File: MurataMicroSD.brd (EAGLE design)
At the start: 60 x 68 mm, 15 parts, among them U1 IC_BLE_LBCA2HNZYZ-711

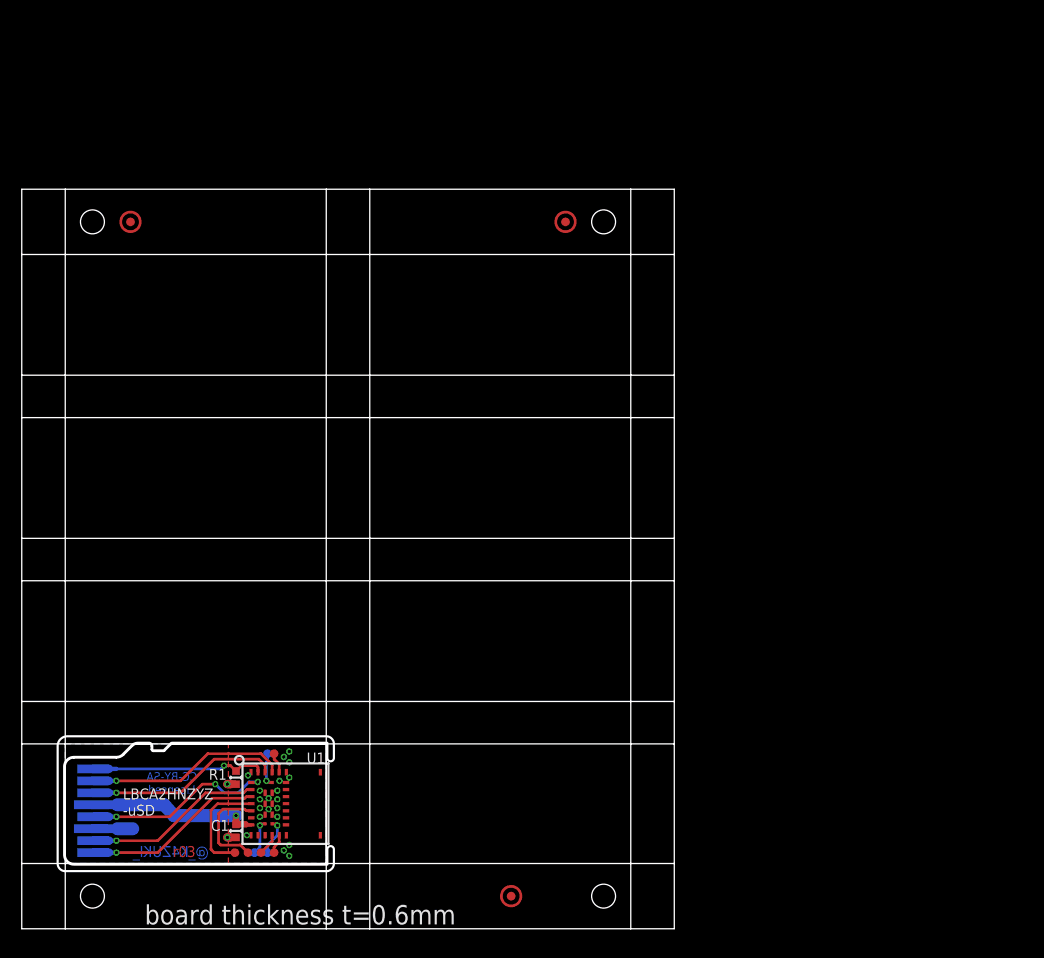
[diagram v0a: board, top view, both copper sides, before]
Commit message: [ FIX ] library update; add debug connector
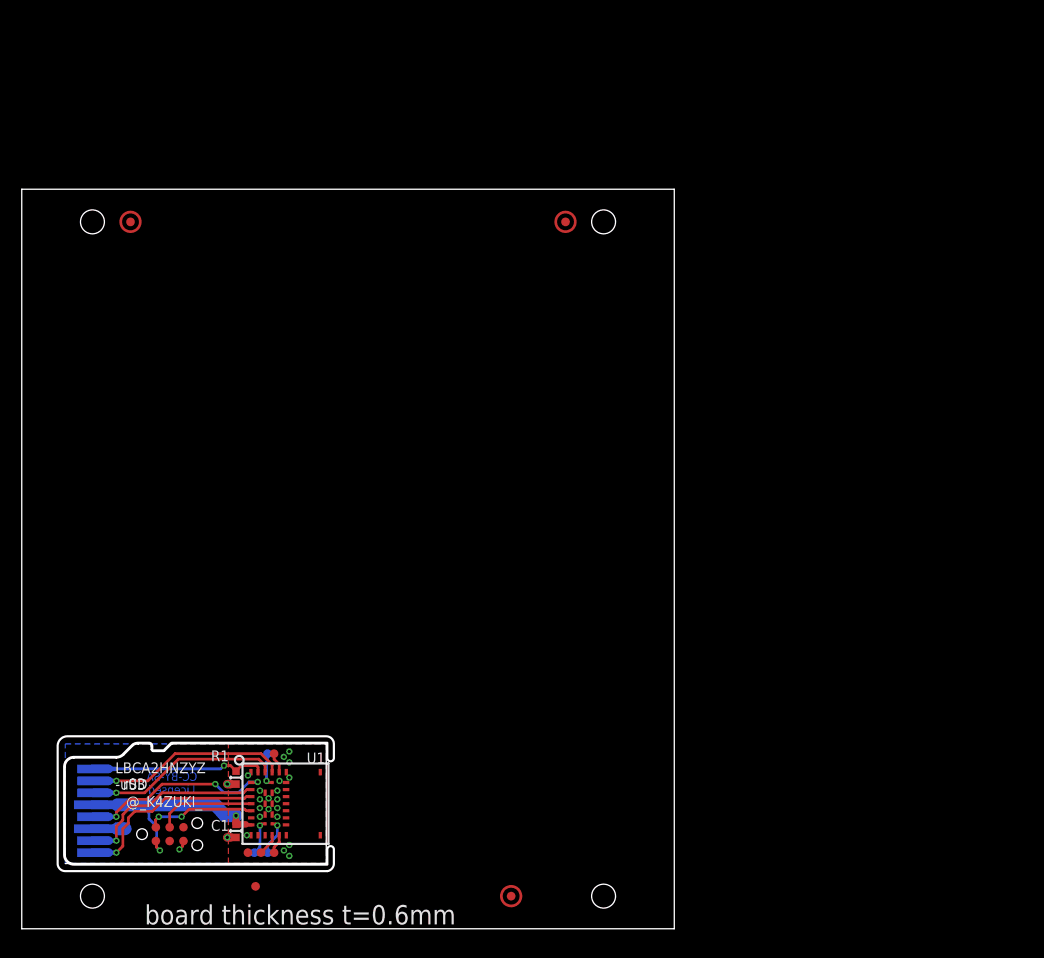
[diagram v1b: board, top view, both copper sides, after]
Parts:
- added CON1: CON_TC2030-CTL-NL, mylib:CON_TC2030-IDC-NL
- moved TP1 3.64 mm to (21.5, 3.90)
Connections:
- net 3.3V: now also CON1.1
- net GND: now also CON1.5
- net SWCLK: now also CON1.4
- net SWDIO: now also CON1.2
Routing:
- net 3.3V: track 16.0 -> 22.6 mm, vias 1 -> 2
- net DAT1: track 16.7 -> 17.9 mm
- net MISO: track 16.5 -> 17.6 mm
- net SWDIO: track 9.00 -> 10.0 mm, vias 0 -> 2
- net SWCLK: track 9.87 -> 9.24 mm
- net GND: track 5.40 -> 5.62 mm, vias 22 -> 23
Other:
- outline, holes or cut-outs redrawn

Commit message: [ uSD ] add 'Open Source Hardware' silk
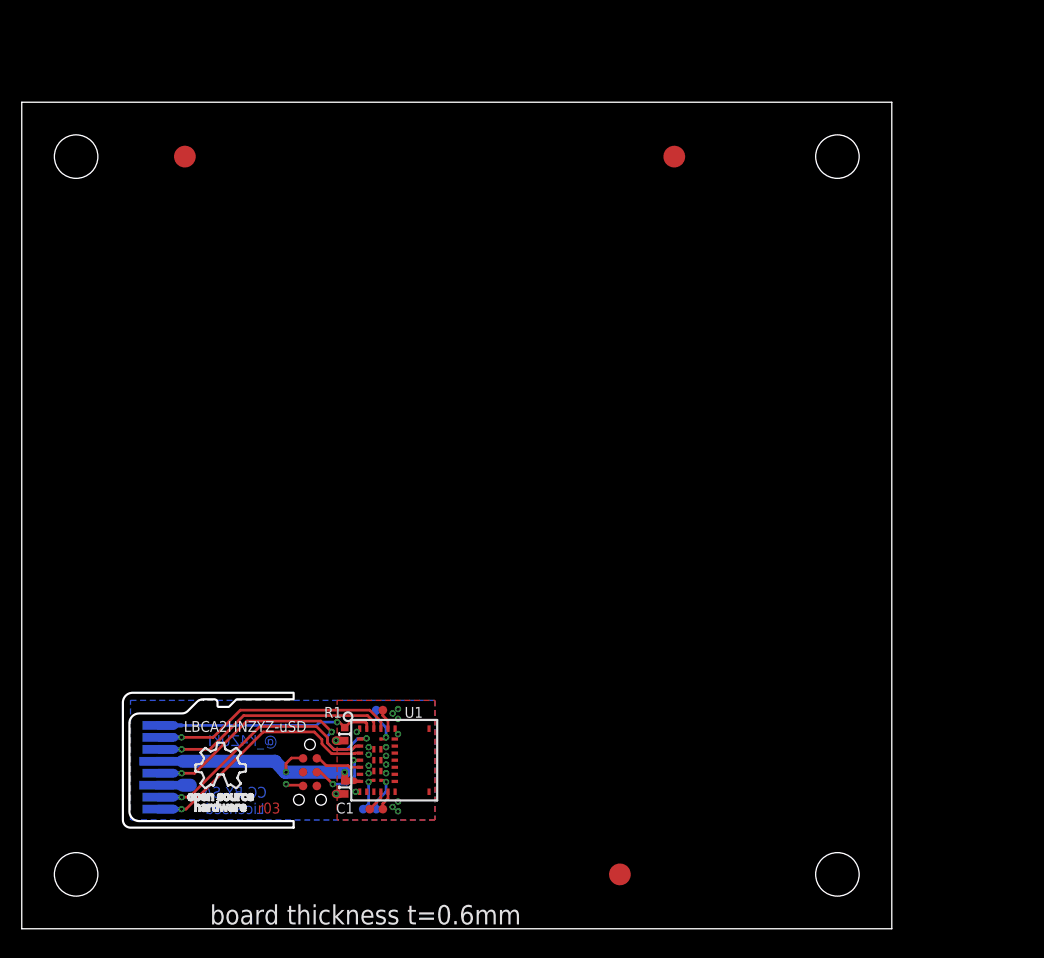
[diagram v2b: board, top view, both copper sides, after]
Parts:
- removed TP1, TP2: TPTP08R, testpad_local:TP08R
- TP3, TP4, TP5: value TPTP08R -> TPTP20R; device testpad_local:TP08R -> testpad_local:TP20R
- moved CON1 14.1 mm to (26.5, 14.4), turned to 270 degrees
- moved TP5 11.7 mm to (60.0, 71.0)
- moved TP8 10.8 mm to (33.2, 11.0)
- moved TP9 10.8 mm to (33.2, 20.1)
- moved C1 10.8 mm to (29.7, 13.0)
- moved TP10 10.8 mm to (32.6, 20.1)
- moved TP11 10.8 mm to (31.4, 11.0)
- moved TP6 10.8 mm to (32.6, 11.0)
- moved TP7 10.8 mm to (32.0, 11.0)
- moved U1 10.8 mm to (30.5, 19.0)
- moved R1 10.8 mm to (29.7, 17.9)
- moved TP4 10.2 mm to (55.0, 5.00)
- moved TP3 7.81 mm to (15.0, 71.0)
- moved C100 7.21 mm to (10.0, 21.0)
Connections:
- net SWCLK: no longer TP1.TP
- net SWDIO: no longer TP2.TP
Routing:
- net SCK: track 18.0 -> 24.4 mm
- net SWDIO: track 10.0 -> 4.33 mm, vias 2 -> 0
- net MISO: track 17.6 -> 22.5 mm
- net DAT1: track 17.9 -> 22.6 mm
- net RXD_MOSI: track 18.0 -> 22.0 mm
- net !CS!: track 18.6 -> 22.6 mm
- net N$1: track 16.2 -> 20.2 mm
- net SWCLK: track 9.24 -> 6.46 mm, vias 0 -> 2
- net GND: track 5.62 -> 6.43 mm, vias 23 -> 20
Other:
- board size 60 x 68 mm -> 80 x 76 mm
- board text added: "LBCA2HNZYZ-uSD"
- board text removed: "LBCA2HNZYZ -uSD"

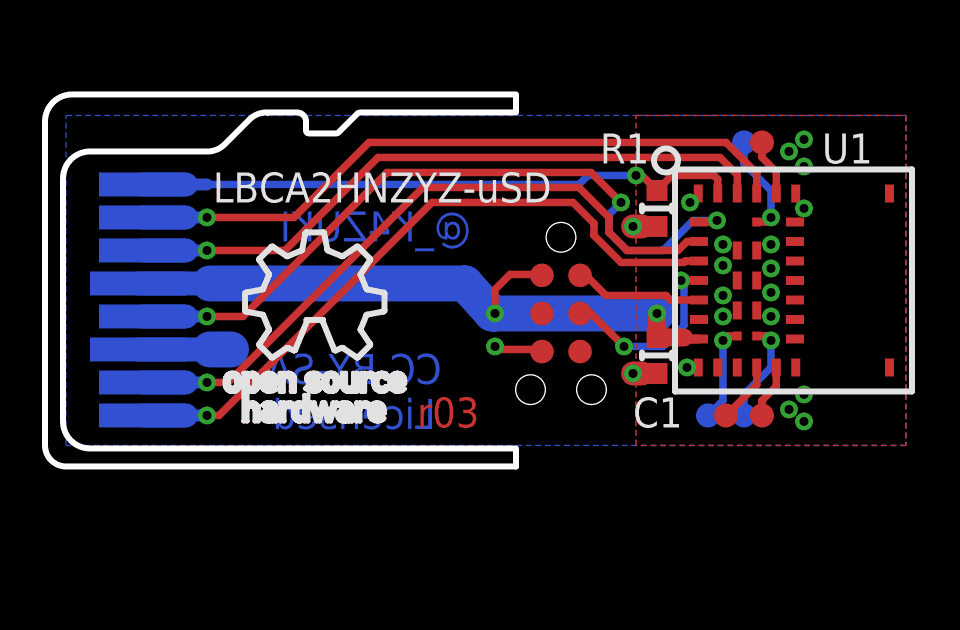
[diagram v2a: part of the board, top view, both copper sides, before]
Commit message: [ uSD ] uSD pin 8 is replaced to Vpp
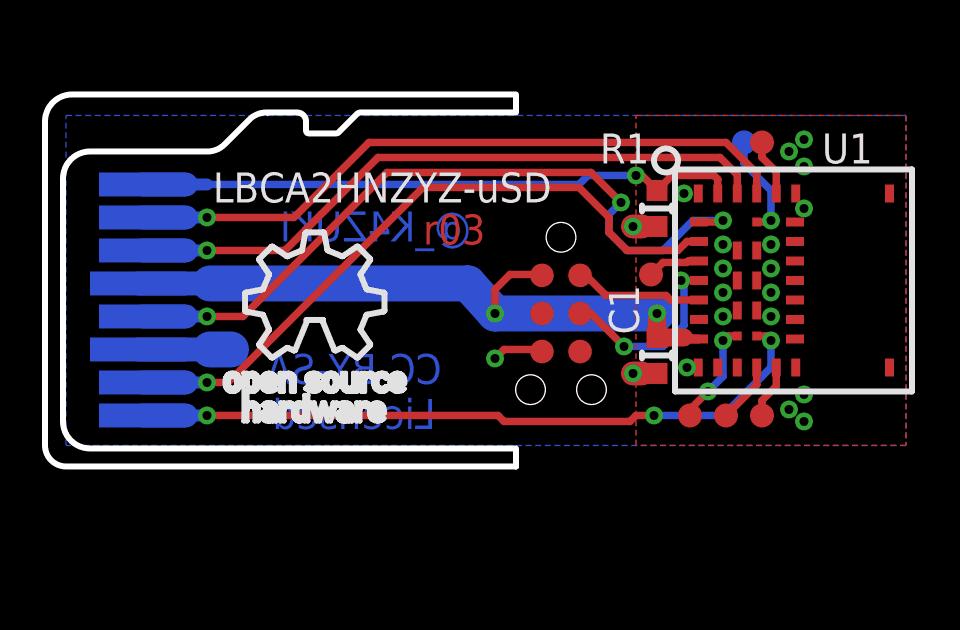
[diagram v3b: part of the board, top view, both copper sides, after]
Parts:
- removed TP6: TPTP08R, testpad_local:TP08R
- added TP1: TPTP08R, testpad_local:TP08R
- moved TP11 0.60 mm to (30.8, 11.0), flipped to the top
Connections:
- net DAT1: now also TP1.TP; no longer C100.8_DAT1
- net N$2: now also C100.8_DAT1; no longer TP6.TP
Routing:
- net DAT1: track 22.6 -> 1.79 mm, vias 1 -> 0
- net N$2: track 3.41 -> 23.2 mm, vias 1 -> 3
- net P1_1: track 3.24 -> 3.49 mm, vias 1 -> 2

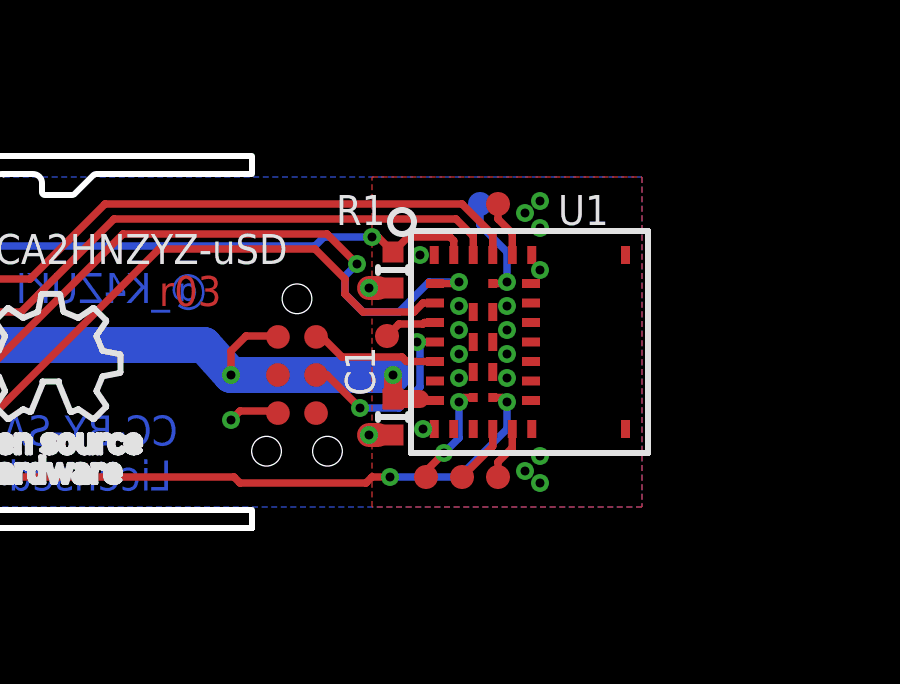
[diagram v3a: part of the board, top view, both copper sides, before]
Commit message: [ uSD ][ USB ] library update
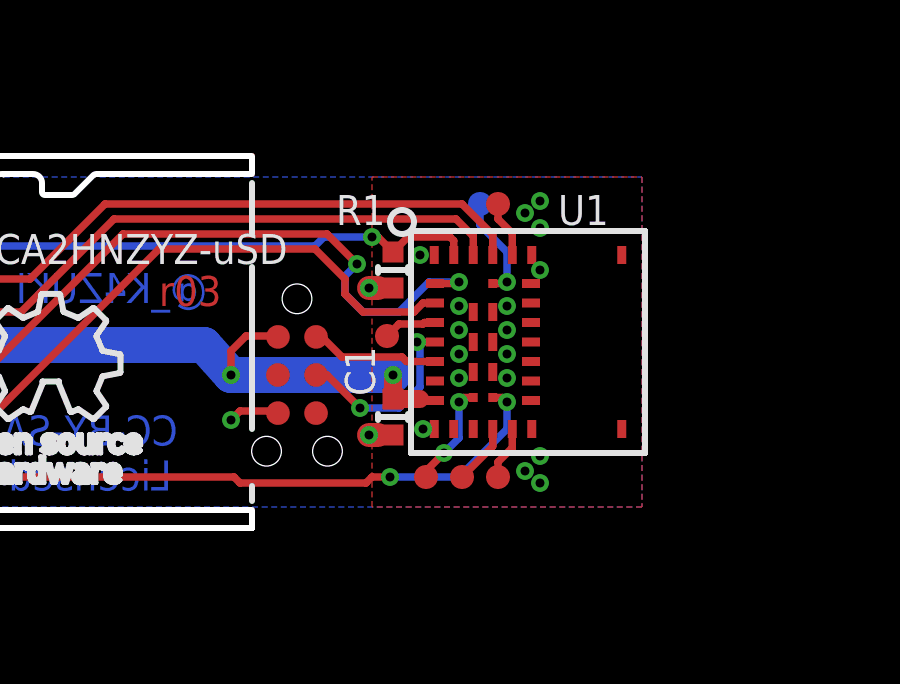
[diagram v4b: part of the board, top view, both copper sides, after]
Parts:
- renumbered TP3 to TP100, TP4 to TP101, TP5 to TP102
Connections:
- net DAT1 renamed P0_6
- net N$2 renamed VPP
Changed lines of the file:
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@@
 <layer number="45" name="Holes" color="7" fill="1" visible="yes" active="yes"/>
 <layer number="46" name="Milling" color="3" fill="0" visible="yes" active="yes"/>
-<layer number="47" name="Measures" color="7" fill="1" visible="yes" active="yes"/>
+<layer number="47" name="Measures" color="7" fill="1" visible="no" active="yes"/>
 <layer number="48" name="Document" color="7" fill="1" visible="no" active="yes"/>
 <layer number="49" name="Reference" color="7" fill="1" visible="no" active="yes"/>
@@
 <wire x1="38" y1="40" x2="38" y2="76" width="0.8" layer="102"/>
 <text x="17.3" y="0.4" size="1.778" layer="25">board thickness t=0.6mm</text>
-<circle x="4" y="30" radius="0.1" width="0.1" layer="51"/>
-<circle x="4" y="45" radius="0.1" width="0.1" layer="51"/>
-<circle x="4" y="60" radius="0.1" width="0.1" layer="51"/>
-<circle x="32" y="60" radius="0.1" width="0.1" layer="51"/>
-<circle x="32" y="45" radius="0.1" width="0.1" layer="51"/>
 <wire x1="10" y1="55" x2="0" y2="55" width="0.8" layer="102"/>
 <wire x1="10" y1="55" x2="70" y2="55" width="0.8" layer="102"/>
 <wire x1="70" y1="55" x2="80" y2="55" width="0.8" layer="102"/>
-<circle x="32" y="30" radius="0.1" width="0.1" layer="51"/>
-<circle x="32" y="15" radius="0.1" width="0.1" layer="51"/>
 <hole x="5" y="5" drill="4"/>
 <hole x="75" y="5" drill="4"/>
@@
 <wire x1="18.944959375" y1="13.181640625" x2="18.55138125" y2="14.14558125" width="0.2" layer="21"/>
 <wire x1="18.55138125" y1="14.14558125" x2="18.566609375" y2="14.18416875" width="0.2" layer="21"/>
+<wire x1="25" y1="20.8" x2="25" y2="19.1" width="0.2" layer="21"/>
+<wire x1="25" y1="18" x2="25" y2="12.6" width="0.2" layer="21"/>
+<wire x1="25" y1="10.7" x2="25" y2="10.2" width="0.2" layer="21"/>
+<dimension x1="38" y1="10" x2="34.9" y2="10" x3="36.45" y3="7.7" textsize="0.999996875" textratio="20" layer="47"/>
 </plain>
 <attributes>
@@
 <attribute name="VALUE" x="31.6" y="17.3" size="1" layer="27" font="vector" ratio="20" rot="R90"/>
 </element>
-<element name="TP3" library="testpad_local" package="TP20R" value="TPTP20R" x="15" y="71" smashed="yes">
+<element name="TP100" library="testpad_local" package="TP20R" value="TPTP20R" x="15" y="71" smashed="yes">
 <attribute name="TP_SIGNAL_NAME" value="" x="15" y="69.095" size="1" layer="37"/>
 <attribute name="VALUE" x="14.619" y="70.619" size="0.0254" layer="27"/>
 </element>
-<element name="TP4" library="testpad_local" package="TP20R" value="TPTP20R" x="55" y="5" smashed="yes">
+<element name="TP101" library="testpad_local" package="TP20R" value="TPTP20R" x="55" y="5" smashed="yes">
 <attribute name="TP_SIGNAL_NAME" value="" x="55" y="3.095" size="1" layer="37"/>
 <attribute name="VALUE" x="54.619" y="4.619" size="0.0254" layer="27"/>
 </element>
-<element name="TP5" library="testpad_local" package="TP20R" value="TPTP20R" x="60" y="71" smashed="yes">
+<element name="TP102" library="testpad_local" package="TP20R" value="TPTP20R" x="60" y="71" smashed="yes">
 <attribute name="TP_SIGNAL_NAME" value="" x="60" y="69.095" size="1" layer="37"/>
 <attribute name="VALUE" x="59.619" y="70.619" size="0.0254" layer="27"/>
@@
 <wire x1="14.7" y1="12.1" x2="14" y2="12.1" width="0.4" layer="16"/>
 </signal>
-<signal name="DAT1">
+<signal name="P0_6">
 <contactref element="U1" pad="3"/>
 <contactref element="TP1" pad="TP"/>
@@
 <wire x1="28" y1="15" x2="30" y2="15" width="0.25" layer="1"/>
 </signal>
-<signal name="N$2">
+<signal name="VPP">
 <contactref element="U1" pad="31"/>
 <wire x1="33.025" y1="13.65" x2="33.35" y2="13.65" width="0.25" layer="1"/>

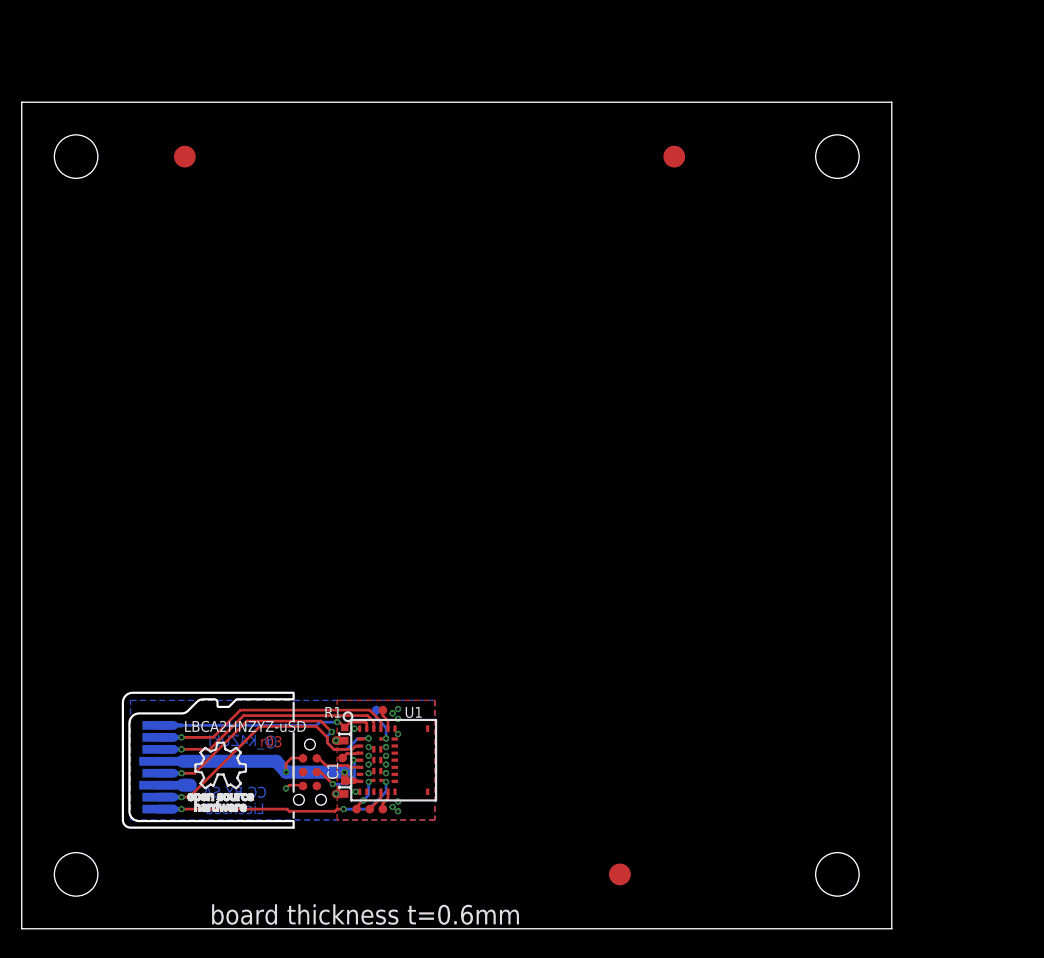
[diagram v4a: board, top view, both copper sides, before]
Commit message: [ FIX ] add SPI ROM; board size extend; silk move
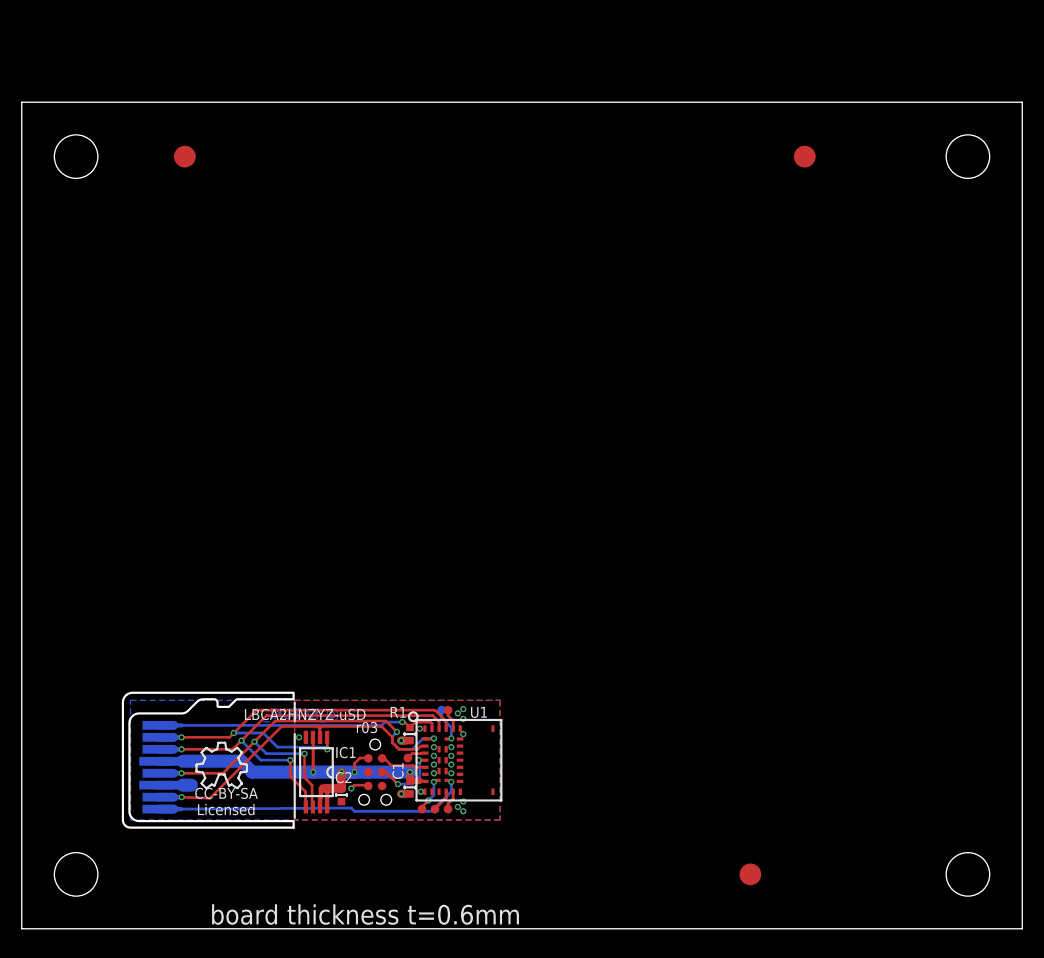
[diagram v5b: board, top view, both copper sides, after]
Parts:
- added C2: (no value), mylib:C0402
- added IC1: IC_SRAM_23K256_256K_32KBST, mylib:IC_08_0.65_160MIL
- moved TP101 12.0 mm to (67.0, 5.00)
- moved TP102 12.0 mm to (72.0, 71.0)
- moved C1 6.00 mm to (35.7, 13.0)
- moved R1 6.00 mm to (35.7, 17.9)
- moved CON1 6.00 mm to (32.5, 14.4)
- moved TP1 6.00 mm to (35.5, 15.7)
- moved TP10 6.00 mm to (38.6, 20.1)
- moved TP7 6.00 mm to (38.0, 11.0)
- moved TP8 6.00 mm to (39.2, 11.0)
- moved TP9 6.00 mm to (39.2, 20.1)
- moved U1 6.00 mm to (36.5, 19.0)
- moved TP11 6.00 mm to (36.8, 11.0)
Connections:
- net !CS!: now also IC1.1
- net 3.3V: now also C2.1, IC1.3, IC1.7, IC1.8
- net GND: now also C2.2, IC1.4
- net MISO: now also IC1.2
- net RXD_MOSI: now also IC1.5
- net SCK: now also IC1.6
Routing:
- net !CS!: track 22.6 -> 38.9 mm, vias 1 -> 3
- net SCK: track 24.8 -> 41.1 mm, vias 3 -> 5
- net RXD_MOSI: track 22.0 -> 38.1 mm, vias 1 -> 3
- net 3.3V: track 22.6 -> 38.3 mm, vias 2 -> 4
- net MISO: track 22.5 -> 30.1 mm
- net VPP: track 23.2 -> 29.5 mm, vias 3 -> 1
- net N$1: track 20.2 -> 26.2 mm
- net GND: track 6.51 -> 6.61 mm, vias 20 -> 21
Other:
- board size 80 x 76 mm -> 92 x 76 mm
